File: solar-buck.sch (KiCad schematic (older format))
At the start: 38 parts, among them J1 PV_input, J2 Conn_02x19_Odd_Even, J3 Conn_02x19_Odd_Even, J4 Batt_output, J5 Load_output, Q1 PMN30ENEA, Q2 PMN30ENEA, SW1 SW_SPST, SW2 SW_Push, SW3 SW_Push, SW4 SW_Push, SW5 SW_Push, SW6 SW_Push, SW7 SW_SPST, U1 L6385E, U2 MAX1614, U3 MAX4378, U4 MIC5233

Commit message: Removed unnessesary labels.
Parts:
- renumbered SW6 to SW2, SW7 to SW3, SW2 to SW4, SW3 to SW5, SW4 to SW6, SW5 to SW7, U4 to U3, U3 to U4
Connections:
- net PA8 is gone; now on net BTN_UP: J3.23 (Pin_23)
- net PA9 is gone; now on net BTN_DOWN: J3.21 (Pin_21)
- net PB6 is gone; now on net BTN_BACK: J3.17 (Pin_17)
- net PC7 is gone; now on net BTN_OK: J3.19 (Pin_19)
- net BTN_UP: now reaches SW4.1
- net BTN_DOWN: now reaches SW5.1
- net BTN_OK: now reaches SW6.1
- net BTN_BACK: now reaches SW7.1
- net BOOT0: no longer names the net of J2.7 (Pin_7)
- net PA0 renamed ACD_solar_I
- net ACD_solar_I: no longer J2.28 (Pin_28)
- net PA1 renamed ADC_buck_I
- net PA10 renamed LCD_D7
- net PA11: no longer names the net of J3.14 (Pin_14)
- net PA12: no longer names the net of J3.12 (Pin_12)
- net PA13: no longer names the net of J2.13 (Pin_13)
- net PA14: no longer names the net of J2.15 (Pin_15)
- net PA15: no longer names the net of J2.17 (Pin_17)
- net PA2: no longer names the net of J3.35 (Pin_35)
- net PA3: no longer names the net of J3.37 (Pin_37)
- net PA4 renamed ADC_load_I
- net PA5: no longer names the net of J3.11 (Pin_11)
- net PA6: no longer names the net of J3.13 (Pin_13)
- net PA7: no longer names the net of J3.15 (Pin_15)
- net PB0 renamed ADC_solar
- net PB1: no longer names the net of J3.24 (Pin_24)
- net PB10 renamed PWM_buck
- net PB11: no longer names the net of J3.18 (Pin_18)
- net PB12: no longer names the net of J3.16 (Pin_16)
- net PB13 renamed LCD_RS
- net PB14: no longer names the net of J3.28 (Pin_28)
- net PB15: no longer names the net of J3.26 (Pin_26)
- net PB2: no longer names the net of J3.22 (Pin_22)
- net PB3 renamed LCD_D6
- net PB4 renamed LCD_D4
- net PB5 renamed LCD_D5
- net PB7: no longer names the net of J2.21 (Pin_21)
- net PB8: no longer names the net of J3.3 (Pin_3)
- net PB9: no longer names the net of J3.5 (Pin_5)
- net PC0: no longer names the net of J2.38 (Pin_38)
- net PC1 renamed ADC_batt
- net PC10: no longer names the net of J2.1 (Pin_1)
- net PC11: no longer names the net of J2.2 (Pin_2)
- net PC12: no longer names the net of J2.3 (Pin_3)
- net PC13 renamed PM_OFF
- net PC14 renamed PM_ON
- net PC15 renamed PM_LBO
- net PC2: no longer names the net of J2.35 (Pin_35)
- net PC3: no longer names the net of J2.37 (Pin_37)
- net PC4 renamed LCD_EN
- net PC5: no longer names the net of J3.6 (Pin_6)
- net PC6: no longer names the net of J3.4 (Pin_4)
- net PC8: no longer names the net of J3.2 (Pin_2)
- net PC9: no longer names the net of J3.1 (Pin_1)
- net PD2: no longer names the net of J2.4 (Pin_4)
- net PH0: no longer names the net of J2.29 (Pin_29)
- net PH1: no longer names the net of J2.31 (Pin_31)
- net VLCD: no longer names the net of J2.33 (Pin_33)
- new net ADC_solar_I: J2.28 (Pin_28)
- no-connect marks 16 -> 50
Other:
- moved on the sheet: C3, C5, C6, C7, J2, J3, SW4, SW5, SW6, SW7, U3

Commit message: Minor changes.
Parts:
- added C10, C8, C9: 1n, symbol Device:C
- added R10, R11, R9: 3.3k, symbol Device:R
- renumbered R2 to R1, R3 to R2, R1 to R3
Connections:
- net ACD_solar_I: now also C8.1, R9.2; no longer U4.1 (OUT1)
- net ADC_buck_I: now also C9.2, R10.1; no longer U4.~ (OUT2)
- net ADC_load_I: now also C10.2, R11.1; no longer U4.8 (OUT3)
- net GND: now also C10.1, C8.2, C9.1
- new net: R9.1, U4.1 (OUT1)
- new net: R11.2, U4.8 (OUT3)
- new net: R10.2, U4.~ (OUT2)
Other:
- moved on the sheet: C5, C6, C7, DS1, R1, R2, R4, R5, R8, RV1, SW3, U3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

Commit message: Lots of changes.
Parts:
- removed C5: 1u, symbol Device:C
- removed C6: 2u2, symbol Device:C
- removed D1: RBR5LAM-30TR, symbol Device:D
- removed Q1, Q2: PMN30ENEA, symbol Device:Q_NMOS_DGS
- removed R6, R7: 30m, symbol Device:R
- removed SW1, SW3: SW_SPST, symbol Switch:SW_SPST
- removed SW2: SW_Push, symbol Switch:SW_Push
- removed U1: L6385E, symbol solar-buck-rescue:L6285E-local
- removed U3: MIC5233, symbol local:MIC5233
- removed U4: MAX4378, symbol solar-buck-rescue:MAX4378-local
- added C1: 10u, Capacitor_SMD:CP_Elec_4x5.4, symbol Device:CP
- added C2: 1u, Capacitor_SMD:C_0805_2012Metric_Pad1.15x1.40mm_HandSolder, symbol Device:C
- added D2: MMSZ5237BT1G, Diode_SMD:D_SOD-123, symbol Device:D_Zener
- added D3: MMSZ5243BT1G, Diode_SMD:D_SOD-123, symbol Device:D_Zener
- added D4: RBR5LAM-30TR, Diode_SMD:D_0805_2012Metric_Pad1.15x1.40mm_HandSolder, symbol Device:D_Schottky
- added J6: LED_ON, Connector_PinHeader_2.54mm:PinHeader_2x01_P2.54mm_Vertical, symbol Connector_Generic:Conn_02x01
- added NT1, NT2, NT3, NT4, NT5, NT6: Net-Tie_2, local:NetTie-2_SMD_Pad8mil, symbol Device:Net-Tie_2
- added Q1, Q2: PMN30ENEA, Package_SO:TSOP-6_1.65x3.05mm_P0.95mm, symbol local:PMN30ENEA
- added Q3, Q4: NX3008PBK, Package_TO_SOT_SMD:SOT-23_Handsoldering, symbol Device:Q_PMOS_GSD
- added R1: 10k, Resistor_SMD:R_0805_2012Metric_Pad1.15x1.40mm_HandSolder, symbol Device:R
- added U1: TS2937, Package_TO_SOT_THT:TO-220-3_Vertical, symbol local:TS2937
- added U3: MCP1804, Package_TO_SOT_SMD:SOT-23-5_HandSoldering, symbol local:MCP1804
- added U4: L6285E, Package_SO:SO-8_3.9x4.9mm_P1.27mm, symbol local:L6285E
- added U5: MAX4378, Package_SO:TSSOP-14_4.4x5mm_P0.65mm, symbol local:MAX4378
- C10, C8, C9: value 1n -> 100n; footprint (none) -> Capacitor_SMD:C_0805_2012Metric_Pad1.15x1.40mm_HandSolder
- C3: renamed from C1; footprint (none) -> Capacitor_SMD:CP_Elec_6.3x5.4
- C6: renamed from C4; footprint (none) -> Capacitor_SMD:CP_Elec_5x5.4
- D1: renamed from D2; footprint (none) -> Diode_SMD:D_0805_2012Metric_Pad1.15x1.40mm_HandSolder
- DS1: footprint Display:WC1602A -> Connector_PinSocket_2.54mm:PinSocket_1x16_P2.54mm_Vertical
- J2, J3: footprint Connector_PinHeader_2.54mm:PinHeader_2x19_P2.54mm_Vertical -> Connector_PinSocket_2.54mm:PinSocket_2x19_P2.54mm_Vertical
- L1: value MCPD5022MT470 -> DTPU033A5; footprint (none) -> local:DTPU033A5
- R10: renamed from R5; value 20k -> 100k; footprint (none) -> Resistor_SMD:R_0805_2012Metric_Pad1.15x1.40mm_HandSolder
- R2: renamed from R8; footprint (none) -> Resistor_SMD:R_0805_2012Metric_Pad1.15x1.40mm_HandSolder
- R3: value 30m -> 10k; footprint (none) -> Resistor_SMD:R_0805_2012Metric_Pad1.15x1.40mm_HandSolder
- R4: renamed from R1; value 51k -> 150k; footprint (none) -> Resistor_SMD:R_0805_2012Metric_Pad1.15x1.40mm_HandSolder
- R5: renamed from R2; value 130k -> 200k; footprint (none) -> Resistor_SMD:R_0805_2012Metric_Pad1.15x1.40mm_HandSolder
- R6: renamed from R9; footprint (none) -> Resistor_SMD:R_0805_2012Metric_Pad1.15x1.40mm_HandSolder
- R7: renamed from R10; footprint (none) -> Resistor_SMD:R_0805_2012Metric_Pad1.15x1.40mm_HandSolder
- R8: renamed from R11; footprint (none) -> Resistor_SMD:R_0805_2012Metric_Pad1.15x1.40mm_HandSolder
- R9: renamed from R4; value 15k -> 120k; footprint (none) -> Resistor_SMD:R_0805_2012Metric_Pad1.15x1.40mm_HandSolder
- RV1: footprint (none) -> Potentiometer_SMD:Potentiometer_Bourns_TC33X_Vertical
- SW1: renamed from SW4; footprint (none) -> Button_Switch_THT:SW_PUSH_6mm
- SW2: renamed from SW5; footprint (none) -> Button_Switch_THT:SW_PUSH_6mm
- SW3: renamed from SW6; footprint (none) -> Button_Switch_THT:SW_PUSH_6mm
- SW4: renamed from SW7; footprint (none) -> Button_Switch_THT:SW_PUSH_6mm
- U2: footprint (none) -> Package_SO:MSOP-8_3x3mm_P0.65mm
- renumbered C2 to C4, C3 to C5, J5 to J4, J4 to J5
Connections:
- net ACD_solar_I is gone; now on net ADC_solar_I: C8.1, R6.2
- net E5V is gone; now on net +5V: J2.6 (Pin_6)
- net +5V: now also R3.2, C1.1, Q3.2 (S), Q4.2 (S), R1.1, U1.3 (OUT); no longer C5.1, C7.1, DS1.2 (VDD), J2.18 (Pin_18), R2.1, RV1.1
- net 6: now also J6.1 (Pin_1)
- net GND: now also J1.2 (Pin_2), C1.2, C2.2, J6.2 (Pin_2), U1.2 (GND), U3.2 (GND), U4.4 (GND), U5.11 (GND); no longer J1.1 (Pin_1)
- net PWM_buck: now also U4.2 (HIN)
- net V_batt: now also U2.8 (BATT), C2.1, D2.1 (K), D4.1 (K), NT3.2, NT4.2, NT5.1, NT6.1, Q1.1 (D), Q1.2 (D), Q1.5 (D), Q1.6 (D), U1.1 (IN); no longer R4.2
- net V_load: now also J4.1 (Pin_1), U2.7 (SRC), Q1.4 (S); no longer U2.8 (BATT)
- net V_solar: now also C3.1, J1.1 (Pin_1), D3.1 (K), NT1.1, NT2.1, Q2.1 (D), Q2.2 (D), Q2.5 (D), Q2.6 (D), U3.1 (VIN); no longer R3.2, R5.2
- net at C4.2, D1.1 (K), L1.1: now also Q2.4 (S), U4.6 (OUT)
- net at C4.1: now also U4.8 (VBOOT)
- net at R6.1: now also U5.1 (OUT1)
- net at R8.2: now also U5.8 (OUT3)
- net at R7.2: now also U5.7 (OUT2)
- net HSCA_SHDN: now reaches J2.35 (Pin_35)
- net HSCA_SHDN: now also R3.1, Q4.1 (G)
- net 12V_SHDN: now reaches J2.37 (Pin_37)
- net 12V_SHDN: now also U3.4 (SHDN)
- net LCD_SHDN: now reaches J2.38 (Pin_38)
- net LCD_SHDN: now also Q3.1 (G), R1.2
- net at U2.6 (GATE): now also Q1.3 (G)
- net +3.3V: no longer names the net of J2.16 (Pin_16)
- net AGND: no longer names the net of J3.32 (Pin_32)
- net AVDD: no longer names the net of J3.7 (Pin_7)
- net IOREF: no longer names the net of J2.12 (Pin_12)
- net RESET: no longer names the net of J2.14 (Pin_14)
- net U5V: no longer names the net of J3.8 (Pin_8)
- net VDD: no longer names the net of J2.5 (Pin_5)
- net VIN: no longer names the net of J2.24 (Pin_24)
- net V_buck: no longer names the net of C6.1, L1.2
- net V_buck: now also D4.2 (A)
- removed net V_solar_-: C3.1, R3.1
- new net: DS1.2 (VDD), Q3.3 (D), R2.1, RV1.1
- new net: D3.2 (A), R5.2
- new net: D2.2 (A), R4.2
- new net: C7.1, Q4.3 (D), U5.4 (VCC)
- new net: C5.1, U3.5 (VOUT), U4.3 (VCC)
- new net: Q2.3 (G), U4.7 (HVG)
- new net V_batt+: NT5.2, U5.10 (RS3+)
- new net V_batt-: NT6.2, U5.9 (RS3-)
- new net V_buck+: U5.5 (R2+)
- new net V_buck-: U5.6 (RS2-)
- new net V_load+: NT4.1
- new net V_load-: NT3.1
- new net V_solar+: NT1.2, U5.3 (RS1+)
- new net V_solar-: NT2.2, U5.2 (RS-)
- no-connect marks 50 -> 56
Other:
- note added: "30 mOhm PCB\nShunt Resistor\n"
- note added: "W obudowie TO-220"
- moved on the sheet: C10, C3, C4, C5, C6, C7, C8, C9, D1, DS1, J1, J4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

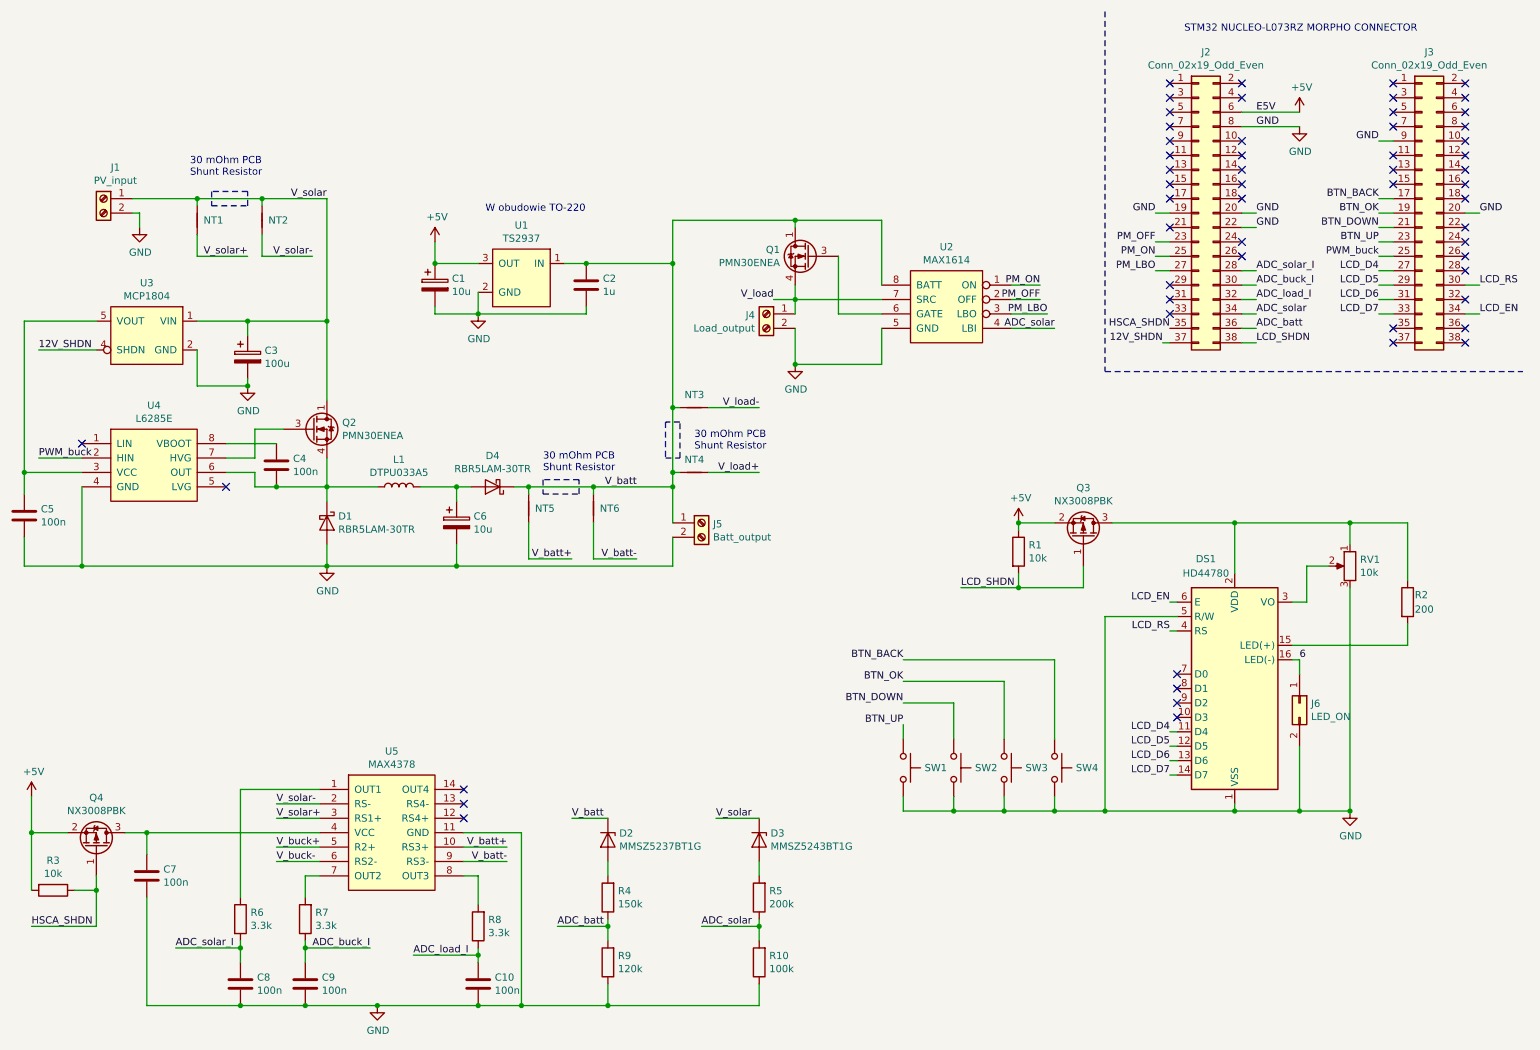
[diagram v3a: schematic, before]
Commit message: I exchanged some components to better ones.
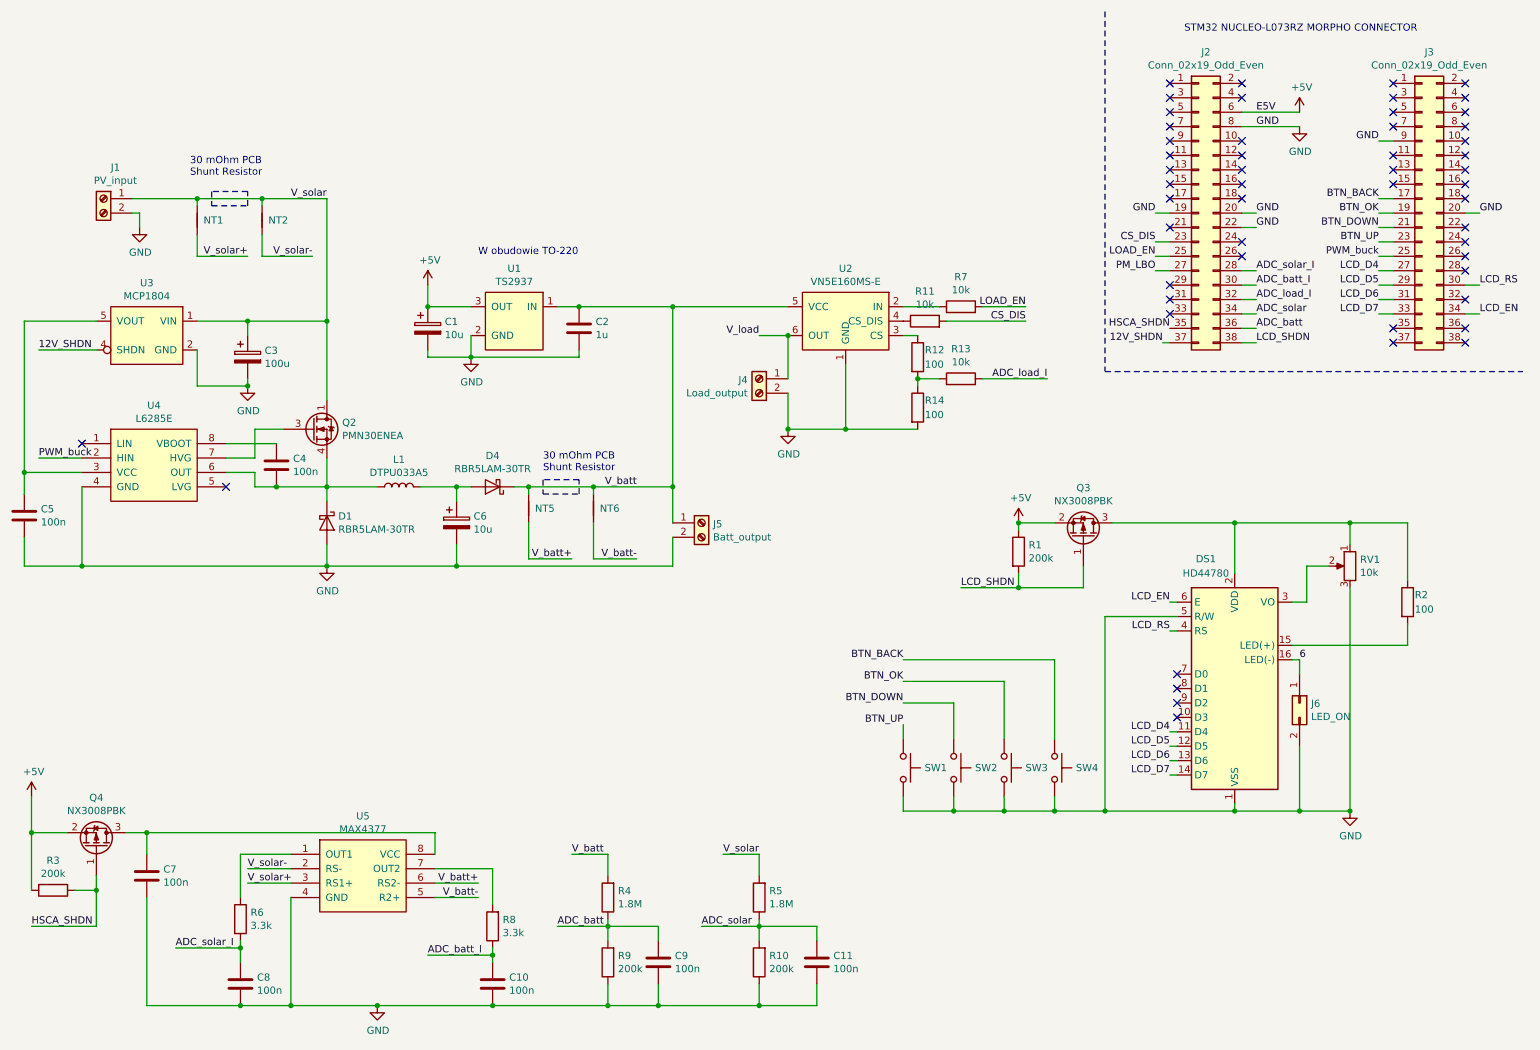
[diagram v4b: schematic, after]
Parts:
- removed D2: MMSZ5237BT1G, Diode_SMD:D_SOD-123, symbol Device:D_Zener
- removed D3: MMSZ5243BT1G, Diode_SMD:D_SOD-123, symbol Device:D_Zener
- removed NT3, NT4: Net-Tie_2, local:NetTie-2_SMD_Pad8mil, symbol Device:Net-Tie_2
- removed Q1: PMN30ENEA, Package_SO:TSOP-6_1.65x3.05mm_P0.95mm, symbol local:PMN30ENEA
- removed U2: MAX1614, Package_SO:MSOP-8_3x3mm_P0.65mm, symbol local:MAX1614
- removed U5: MAX4378, Package_SO:TSSOP-14_4.4x5mm_P0.65mm, symbol local:MAX4378
- added C11: 100n, Capacitor_SMD:C_0805_2012Metric_Pad1.15x1.40mm_HandSolder, symbol Device:C
- added R11, R13: 10k, Resistor_SMD:R_0805_2012Metric_Pad1.15x1.40mm_HandSolder, symbol Device:R
- added R12, R14: 100, Resistor_SMD:R_0805_2012Metric_Pad1.15x1.40mm_HandSolder, symbol Device:R
- added U2: VN5E160MS-E, symbol local:VN5E160MS-E
- added U5: MAX4377, symbol local:MAX4377
- R1, R3: value 10k -> 200k
- R10: value 100k -> 200k
- R2: value 200 -> 100
- R4: value 150k -> 1.8M
- R5: value 200k -> 1.8M
- R7: value 3.3k -> 10k
- R9: value 120k -> 200k
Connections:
- net PM_ON is gone; now on net LOAD_EN: J2.25 (Pin_25)
- net ADC_batt: now also C9.2
- net ADC_load_I: now also R13.2; no longer C10.2, R8.1
- net ADC_solar: now also C11.2
- net GND: now also C11.1, R14.2, U2.1 (GND), U5.4 (GND)
- net V_batt: now also R4.2, U2.5 (VCC), U2.8 (VCC)
- net V_batt+: now also U5.6 (RS2-)
- net V_batt-: now also U5.5 (R2+)
- net V_load: now also U2.6 (OUT), U2.7 (OUT)
- net V_solar: now also R5.2
- net V_solar+: now also U5.3 (RS1+)
- net V_solar-: now also U5.2 (RS-)
- net at C7.1, Q4.3 (D): now also U5.8 (VCC)
- net LOAD_EN: now reaches R7.2
- net at R8.2: now also U5.7 (OUT2)
- net at R6.1: now also U5.1 (OUT1)
- removed net ADC_buck_I: C9.2, J2.30 (Pin_30), R7.1
- net PM_OFF renamed CS_DIS
- net CS_DIS: now also R11.2
- new net: R7.1, U2.2 (IN)
- new net: R12.1, U2.3 (CS)
- new net: R11.1, U2.4 (CS_DIS)
- new net: R12.2, R13.1, R14.1
- new net ADC_batt_I: C10.2, J2.30 (Pin_30), R8.1
- no-connect marks 56 -> 53
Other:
- moved on the sheet: C1, C10, C2, J4, R8, U1
